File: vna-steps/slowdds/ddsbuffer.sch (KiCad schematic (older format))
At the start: 3 parts

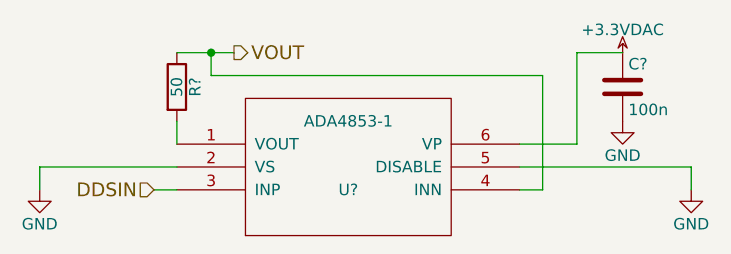
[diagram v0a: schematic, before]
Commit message: slowdds layout completed. images + schematics generated. ZIP file scripts added and documented in README. slowdds gerbers generated + zipped.
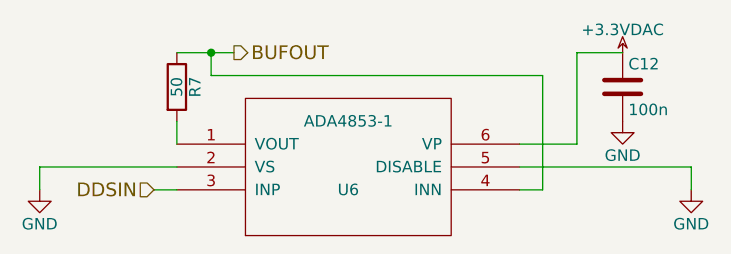
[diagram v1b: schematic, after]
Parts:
- C12: renamed from C?; footprint (none) -> Capacitors_SMD:C_0402
- R7: renamed from R?; footprint (none) -> Resistors_SMD:R_0603
- U6: renamed from U?; footprint MODULE -> Housings_SOT-23_SOT-143_TSOT-6:SC-70-6
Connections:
- net VOUT renamed BUFOUT
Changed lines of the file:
@@
 $EndDescr
 $Comp
-L ADA4853-1 U?
+L ADA4853-1 U6
 U 1 1 55855BA9
 P 5450 3600
-F 0 "U?" H 5450 3500 50  0000 C CNN
+F 0 "U6" H 5450 3500 50  0000 C CNN
 F 1 "ADA4853-1" H 5450 3800 50  0000 C CNN
-F 2 "MODULE" H 5450 3800 50  0001 C CNN
+F 2 "Housings_SOT-23_SOT-143_TSOT-6:SC-70-6" H 5450 3800 50  0001 C CNN
 F 3 "DOCUMENTATION" H 5450 3400 50  0001 C CNN
 	1    5450 3600
@@
 $EndComp
 $Comp
-L GND #PWR?
+L GND #PWR035
 U 1 1 55855BE6
 P 4100 3700
-F 0 "#PWR?" H 4100 3450 50  0001 C CNN
+F 0 "#PWR035" H 4100 3450 50  0001 C CNN
 F 1 "GND" H 4100 3550 50  0000 C CNN
 F 2 "" H 4100 3700 60  0000 C CNN
@@
 	4600 3700 4700 3700
 $Comp
-L C C?
+L C C12
 U 1 1 55855C2E
 P 6650 3250
-F 0 "C?" H 6675 3350 50  0000 L CNN
+F 0 "C12" H 6675 3350 50  0000 L CNN
 F 1 "100n" H 6675 3150 50  0000 L CNN
-F 2 "" H 6688 3100 30  0000 C CNN
+F 2 "Capacitors_SMD:C_0402" H 6688 3100 30  0001 C CNN
 F 3 "" H 6650 3250 60  0000 C CNN
 	1    6650 3250
@@
 $EndComp
 $Comp
-L GND #PWR?
+L GND #PWR036
 U 1 1 55855C6B
 P 6650 3400
-F 0 "#PWR?" H 6650 3150 50  0001 C CNN
+F 0 "#PWR036" H 6650 3150 50  0001 C CNN
 F 1 "GND" H 6650 3250 50  0000 C CNN
 F 2 "" H 6650 3400 60  0000 C CNN
@@
 $EndComp
 $Comp
-L GND #PWR?
+L GND #PWR037
 U 1 1 55855C93
 P 6950 3700
-F 0 "#PWR?" H 6950 3450 50  0001 C CNN
+F 0 "#PWR037" H 6950 3450 50  0001 C CNN
 F 1 "GND" H 6950 3550 50  0000 C CNN
 F 2 "" H 6950 3700 60  0000 C CNN
@@
 	6450 3100 6650 3100
 $Comp
-L +3.3VDAC #PWR?
+L +3.3VDAC #PWR038
 U 1 1 55855CB3
 P 6650 3100
-F 0 "#PWR?" H 6800 3050 50  0001 C CNN
+F 0 "#PWR038" H 6800 3050 50  0001 C CNN
 F 1 "+3.3VDAC" H 6650 3200 50  0000 C CNN
 F 2 "" H 6650 3100 60  0000 C CNN
@@
 $EndComp
 $Comp
-L R R?
+L R R7
 U 1 1 55855CE6
 P 4700 3250
-F 0 "R?" V 4780 3250 50  0000 C CNN
+F 0 "R7" V 4780 3250 50  0000 C CNN
 F 1 "50" V 4700 3250 50  0000 C CNN
-F 2 "" V 4630 3250 30  0000 C CNN
+F 2 "Resistors_SMD:R_0603" V 4630 3250 30  0001 C CNN
 F 3 "" H 4700 3250 30  0000 C CNN
 	1    4700 3250
@@
 	4700 3500 4700 3400
 Text HLabel 4950 3100 2    60   Output ~ 0
-VOUT
+BUFOUT
 Wire Wire Line
 	4700 3100 4950 3100
